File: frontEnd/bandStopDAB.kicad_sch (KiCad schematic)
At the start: 18 parts, among them U401 BGS12P2L6E6327XTSA1, U402 BGS12P2L6E6327XTSA1

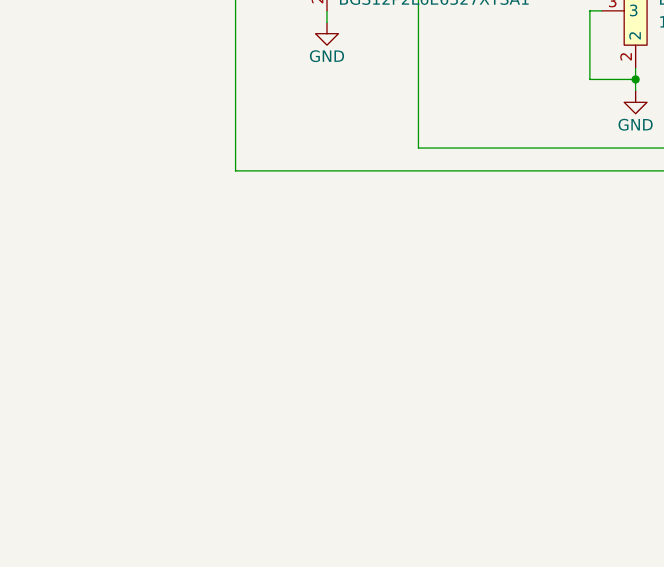
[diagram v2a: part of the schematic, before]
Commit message: add leds for each filter block
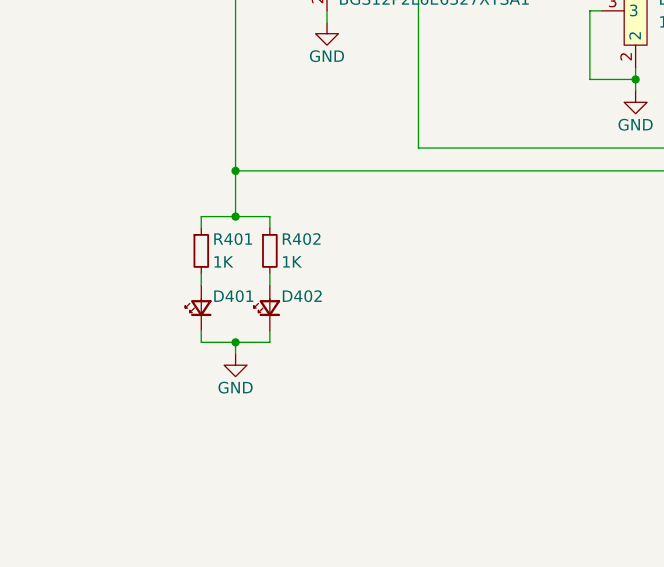
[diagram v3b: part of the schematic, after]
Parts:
- added D401, D402: LED_Small, LED_SMD:LED_0805_2012Metric, symbol Device:LED_Small
- added R401, R402: 1K, Resistor_SMD:R_0805_2012Metric, symbol Device:R_Small
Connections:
- net FILTER_ENABLE: now also R401.1, R402.1
- net GND: now also D401.1 (K), D402.1 (K)
- new net: D401.2 (A), R401.2
- new net: D402.2 (A), R402.2
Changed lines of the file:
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@@
 (kicad_sch (version 20211123) (generator eeschema)
   (paper "A4")
+  (junction (at 60.96 125.73) (diameter 0) (color 0 0 0 0)
+  )
   (junction (at 114.3 74.93) (diameter 0) (color 0 0 0 0)
   )
@@
   (junction (at 180.34 74.93) (diameter 0) (color 0 0 0 0)
   )
+  (junction (at 60.96 106.68) (diameter 0) (color 0 0 0 0)
+  )
   (junction (at 44.45 180.34) (diameter 0) (color 0 0 0 0)
   )
@@
   (junction (at 44.45 172.72) (diameter 0) (color 0 0 0 0)
   )
+  (junction (at 60.96 111.76) (diameter 0) (color 0 0 0 0)
+  )
   (junction (at 204.47 96.52) (diameter 0) (color 0 0 0 0)
   )
@@
     (stroke (width 0) (type default) (color 0 0 0 0))
   )
+  (wire (pts (xy 60.96 106.68) (xy 60.96 111.76))
+    (stroke (width 0) (type default) (color 0 0 0 0))
+  )
   (wire (pts (xy 129.54 81.28) (xy 129.54 74.93))
     (stroke (width 0) (type default) (color 0 0 0 0))
@@
     (stroke (width 0) (type default) (color 0 0 0 0))
   )
+  (wire (pts (xy 57.15 113.03) (xy 57.15 111.76))
+    (stroke (width 0) (type default) (color 0 0 0 0))
+  )
+  (wire (pts (xy 57.15 118.11) (xy 57.15 119.38))
+    (stroke (width 0) (type default) (color 0 0 0 0))
+  )
   (wire (pts (xy 129.54 74.93) (xy 138.43 74.93))
     (stroke (width 0) (type default) (color 0 0 0 0))
@@
     (stroke (width 0) (type default) (color 0 0 0 0))
   )
+  (wire (pts (xy 57.15 125.73) (xy 60.96 125.73))
+    (stroke (width 0) (type default) (color 0 0 0 0))
+  )
   (wire (pts (xy 162.56 71.12) (xy 162.56 74.93))
     (stroke (width 0) (type default) (color 0 0 0 0))
@@
     (stroke (width 0) (type default) (color 0 0 0 0))
   )
+  (wire (pts (xy 60.96 125.73) (xy 60.96 127))
+    (stroke (width 0) (type default) (color 0 0 0 0))
+  )
   (wire (pts (xy 204.47 95.25) (xy 204.47 96.52))
     (stroke (width 0) (type default) (color 0 0 0 0))
@@
     (stroke (width 0) (type default) (color 0 0 0 0))
   )
+  (wire (pts (xy 64.77 111.76) (xy 64.77 113.03))
+    (stroke (width 0) (type default) (color 0 0 0 0))
+  )
+  (wire (pts (xy 60.96 111.76) (xy 64.77 111.76))
+    (stroke (width 0) (type default) (color 0 0 0 0))
+  )
   (wire (pts (xy 134.62 88.9) (xy 133.35 88.9))
     (stroke (width 0) (type default) (color 0 0 0 0))
@@
     (stroke (width 0) (type default) (color 0 0 0 0))
   )
+  (wire (pts (xy 64.77 124.46) (xy 64.77 125.73))
+    (stroke (width 0) (type default) (color 0 0 0 0))
+  )
   (wire (pts (xy 44.45 180.34) (xy 44.45 181.61))
     (stroke (width 0) (type default) (color 0 0 0 0))
@@
     (stroke (width 0) (type default) (color 0 0 0 0))
   )
+  (wire (pts (xy 60.96 125.73) (xy 64.77 125.73))
+    (stroke (width 0) (type default) (color 0 0 0 0))
+  )
   (wire (pts (xy 229.87 88.9) (xy 229.87 90.17))
     (stroke (width 0) (type default) (color 0 0 0 0))
@@
     (stroke (width 0) (type default) (color 0 0 0 0))
   )
+  (wire (pts (xy 64.77 118.11) (xy 64.77 119.38))
+    (stroke (width 0) (type default) (color 0 0 0 0))
+  )
   (wire (pts (xy 195.58 71.12) (xy 195.58 74.93))
     (stroke (width 0) (type default) (color 0 0 0 0))
@@
     (stroke (width 0) (type default) (color 0 0 0 0))
   )
+  (wire (pts (xy 57.15 111.76) (xy 60.96 111.76))
+    (stroke (width 0) (type default) (color 0 0 0 0))
+  )
   (wire (pts (xy 194.31 81.28) (xy 195.58 81.28))
     (stroke (width 0) (type default) (color 0 0 0 0))
@@
   )
   (wire (pts (xy 171.45 96.52) (xy 171.45 97.79))
+    (stroke (width 0) (type default) (color 0 0 0 0))
+  )
+  (wire (pts (xy 57.15 124.46) (xy 57.15 125.73))
     (stroke (width 0) (type default) (color 0 0 0 0))
   )
@@
     (pin "2")
   )
+  (symbol (lib_id "power:GND") (at 60.96 127 0) (unit 1)
+    (in_bom yes) (on_board yes)
+    (property "Reference" "#PWR?" (id 0) (at 60.96 133.35 0)
+      (effects (font (size 1.27 1.27)) hide)
+    )
+    (property "Value" "GND" (id 1) (at 60.96 130.81 0))
+    (property "Footprint" "" (id 2) (at 60.96 127 0)
+      (effects (font (size 1.27 1.27)) hide)
+    )
+    (property "Datasheet" "" (id 3) (at 60.96 127 0)
+      (effects (font (size 1.27 1.27)) hide)
+    )
+    (pin "1")
+  )
   (symbol (lib_id "frontEnd:DIY_COIL") (at 154.94 81.28 0) (unit 1)
     (in_bom yes) (on_board yes)
@@
     (pin "1")
   )
+  (symbol (lib_id "Device:R_Small") (at 57.15 115.57 0) (unit 1)
+    (in_bom yes) (on_board yes)
+    (property "Reference" "R401" (id 0) (at 58.42 114.3 0)
+      (effects (font (size 1.27 1.27)) (justify left))
+    )
+    (property "Value" "1K" (id 1) (at 58.42 116.84 0)
+      (effects (font (size 1.27 1.27)) (justify left))
+    )
+    (property "Footprint" "Resistor_SMD:R_0805_2012Metric" (id 2) (at 57.15 115.57 0)
+      (effects (font (size 1.27 1.27)) hide)
+    )
+    (property "Datasheet" "~" (id 3) (at 57.15 115.57 0)
+      (effects (font (size 1.27 1.27)) hide)
+    )
+    (pin "1")
+    (pin "2")
+  )
   (symbol (lib_id "frontEnd:DIY_COIL") (at 121.92 81.28 0) (unit 1)
     (in_bom yes) (on_board yes)
@@
     (pin "2")
     (pin "3")
+  )
+  (symbol (lib_id "Device:LED_Small") (at 57.15 121.92 90) (unit 1)
+    (in_bom yes) (on_board yes)
+    (property "Reference" "D401" (id 0) (at 58.42 120.65 90)
+      (effects (font (size 1.27 1.27)) (justify right))
+    )
+    (property "Value" "LED_Small" (id 1) (at 59.69 123.1264 90)
+      (effects (font (size 1.27 1.27)) (justify right) hide)
+    )
+    (property "Footprint" "LED_SMD:LED_0805_2012Metric" (id 2) (at 57.15 121.92 90)
+      (effects (font (size 1.27 1.27)) hide)
+    )
+    (property "Datasheet" "~" (id 3) (at 57.15 121.92 90)
+      (effects (font (size 1.27 1.27)) hide)
+    )
+    (pin "1")
+    (pin "2")
   )
   (symbol (lib_id "Device:C_Small") (at 171.45 78.74 0) (unit 1)
@@
     (pin "2")
   )
+  (symbol (lib_id "Device:LED_Small") (at 64.77 121.92 90) (unit 1)
+    (in_bom yes) (on_board yes)
+    (property "Reference" "D402" (id 0) (at 66.04 120.65 90)
+      (effects (font (size 1.27 1.27)) (justify right))
+    )
+    (property "Value" "LED_Small" (id 1) (at 67.31 123.1264 90)
+      (effects (font (size 1.27 1.27)) (justify right) hide)
+    )
+    (property "Footprint" "LED_SMD:LED_0805_2012Metric" (id 2) (at 64.77 121.92 90)
+      (effects (font (size 1.27 1.27)) hide)
+    )
+    (property "Datasheet" "~" (id 3) (at 64.77 121.92 90)
+      (effects (font (size 1.27 1.27)) hide)
+    )
+    (pin "1")
+    (pin "2")
+  )
   (symbol (lib_id "frontEnd:BGS12P2L6E6327XTSA1") (at 236.22 77.47 0) (mirror y) (unit 1)
     (in_bom yes) (on_board yes)
@@
       (effects (font (size 1.27 1.27)) hide)
     )
+    (pin "1")
+    (pin "2")
+  )
+  (symbol (lib_id "Device:R_Small") (at 64.77 115.57 0) (unit 1)
+    (in_bom yes) (on_board yes)
+    (property "Reference" "R402" (id 0) (at 66.04 114.3 0)
+      (effects (font (size 1.27 1.27)) (justify left))
+    )
+    (property "Value" "1K" (id 1) (at 66.04 116.84 0)
+      (effects (font (size 1.27 1.27)) (justify left))
+    )
+    (property "Footprint" "Resistor_SMD:R_0805_2012Metric" (id 2) (at 64.77 115.57 0)
+      (effects (font (size 1.27 1.27)) hide)
+    )
+    (property "Datasheet" "~" (id 3) (at 64.77 115.57 0)
+      (effects (font (size 1.27 1.27)) hide)
+    )

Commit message: assign footprints, part designators
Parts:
- U401, U402: footprint (none) -> frontEnd:BGS12P2L6E6327XTSA1
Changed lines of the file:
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@@
   (symbol (lib_id "power:GND") (at 60.96 127 0) (unit 1)
     (in_bom yes) (on_board yes)
-    (property "Reference" "#PWR?" (id 0) (at 60.96 133.35 0)
+    (property "Reference" "#PWR0175" (id 0) (at 60.96 133.35 0)
       (effects (font (size 1.27 1.27)) hide)
     )
@@
   (symbol (lib_id "power:GND") (at 187.96 86.36 0) (unit 1)
     (in_bom yes) (on_board yes)
-    (property "Reference" "#PWR?" (id 0) (at 187.96 92.71 0)
+    (property "Reference" "#PWR0164" (id 0) (at 187.96 92.71 0)
       (effects (font (size 1.27 1.27)) hide)
     )
@@
   (symbol (lib_id "power:+3V3") (at 44.45 171.45 0) (unit 1)
     (in_bom yes) (on_board yes)
-    (property "Reference" "#PWR?" (id 0) (at 44.45 175.26 0)
+    (property "Reference" "#PWR0174" (id 0) (at 44.45 175.26 0)
       (effects (font (size 1.27 1.27)) hide)
     )
@@
   (symbol (lib_id "power:GND") (at 171.45 97.79 0) (unit 1)
     (in_bom yes) (on_board yes)
-    (property "Reference" "#PWR?" (id 0) (at 171.45 104.14 0)
+    (property "Reference" "#PWR0171" (id 0) (at 171.45 104.14 0)
       (effects (font (size 1.27 1.27)) hide)
     )
@@
   (symbol (lib_id "power:GND") (at 44.45 181.61 0) (unit 1)
     (in_bom yes) (on_board yes)
-    (property "Reference" "#PWR?" (id 0) (at 44.45 187.96 0)
+    (property "Reference" "#PWR0173" (id 0) (at 44.45 187.96 0)
       (effects (font (size 1.27 1.27)) hide)
     )
@@
   (symbol (lib_id "power:+3V3") (at 229.87 68.58 0) (unit 1)
     (in_bom yes) (on_board yes)
-    (property "Reference" "#PWR?" (id 0) (at 229.87 72.39 0)
+    (property "Reference" "#PWR0162" (id 0) (at 229.87 72.39 0)
       (effects (font (size 1.27 1.27)) hide)
     )
@@
   (symbol (lib_id "power:GND") (at 204.47 97.79 0) (unit 1)
     (in_bom yes) (on_board yes)
-    (property "Reference" "#PWR?" (id 0) (at 204.47 104.14 0)
+    (property "Reference" "#PWR0169" (id 0) (at 204.47 104.14 0)
       (effects (font (size 1.27 1.27)) hide)
     )
@@
       (effects (font (size 1.27 1.27)) (justify left))
     )
-    (property "Footprint" "" (id 2) (at 64.77 77.47 0)
+    (property "Footprint" "frontEnd:BGS12P2L6E6327XTSA1" (id 2) (at 64.77 77.47 0)
       (effects (font (size 1.27 1.27)) hide)
     )
@@
   (symbol (lib_id "power:GND") (at 154.94 86.36 0) (unit 1)
     (in_bom yes) (on_board yes)
-    (property "Reference" "#PWR?" (id 0) (at 154.94 92.71 0)
+    (property "Reference" "#PWR0168" (id 0) (at 154.94 92.71 0)
       (effects (font (size 1.27 1.27)) hide)
     )
@@
   (symbol (lib_id "power:GND") (at 138.43 97.79 0) (unit 1)
     (in_bom yes) (on_board yes)
-    (property "Reference" "#PWR?" (id 0) (at 138.43 104.14 0)
+    (property "Reference" "#PWR0170" (id 0) (at 138.43 104.14 0)
       (effects (font (size 1.27 1.27)) hide)
     )
@@
       (effects (font (size 1.27 1.27)) (justify right))
     )
-    (property "Footprint" "" (id 2) (at 236.22 77.47 0)
+    (property "Footprint" "frontEnd:BGS12P2L6E6327XTSA1" (id 2) (at 236.22 77.47 0)
       (effects (font (size 1.27 1.27)) hide)
     )
@@
   (symbol (lib_id "power:GND") (at 121.92 86.36 0) (unit 1)
     (in_bom yes) (on_board yes)
-    (property "Reference" "#PWR?" (id 0) (at 121.92 92.71 0)
+    (property "Reference" "#PWR0165" (id 0) (at 121.92 92.71 0)
       (effects (font (size 1.27 1.27)) hide)
     )
@@
   (symbol (lib_id "power:+3V3") (at 71.12 68.58 0) (unit 1)
     (in_bom yes) (on_board yes)
-    (property "Reference" "#PWR?" (id 0) (at 71.12 72.39 0)
+    (property "Reference" "#PWR0166" (id 0) (at 71.12 72.39 0)
       (effects (font (size 1.27 1.27)) hide)
     )
@@
   (symbol (lib_id "power:GND") (at 105.41 97.79 0) (unit 1)
     (in_bom yes) (on_board yes)
-    (property "Reference" "#PWR?" (id 0) (at 105.41 104.14 0)
+    (property "Reference" "#PWR0172" (id 0) (at 105.41 104.14 0)
       (effects (font (size 1.27 1.27)) hide)
     )
@@
   (symbol (lib_id "power:GND") (at 229.87 90.17 0) (unit 1)
     (in_bom yes) (on_board yes)
-    (property "Reference" "#PWR?" (id 0) (at 229.87 96.52 0)
+    (property "Reference" "#PWR0163" (id 0) (at 229.87 96.52 0)
       (effects (font (size 1.27 1.27)) hide)
     )
@@
   (symbol (lib_id "power:GND") (at 71.12 90.17 0) (unit 1)
     (in_bom yes) (on_board yes)
-    (property "Reference" "#PWR?" (id 0) (at 71.12 96.52 0)
-      (effects (font (size 1.27 1.27)) hide)
-    )
+    (property "Reference" "#PWR0167" (id 0) (at 71.12 96.52 0)
+      (effects (font (size 1.27 1.27)) hide)
+    )

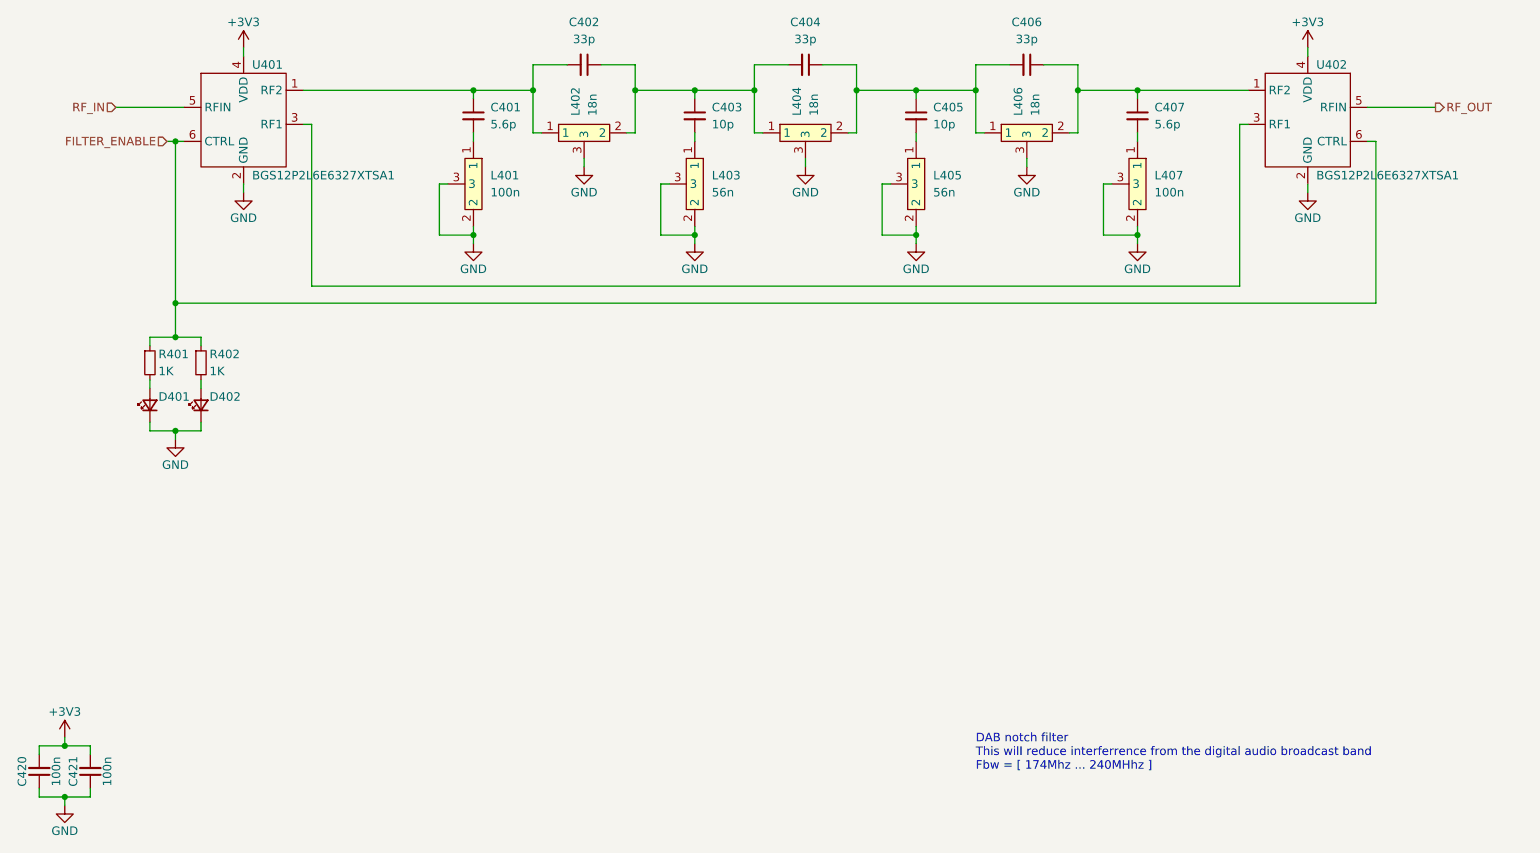
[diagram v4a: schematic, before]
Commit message: convert all embeded filter to plug-in modules, start pcb layout
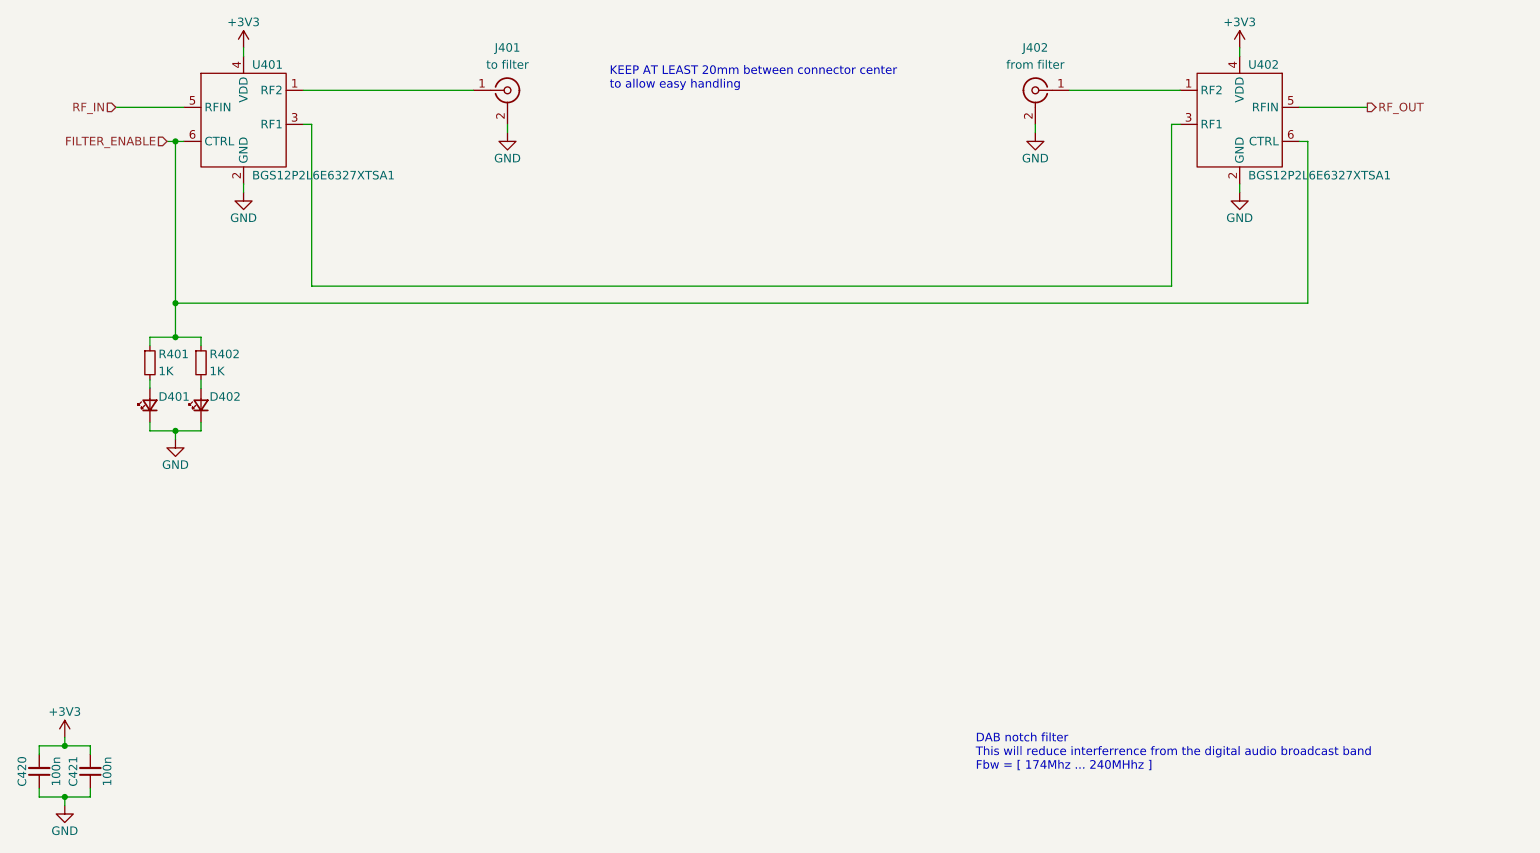
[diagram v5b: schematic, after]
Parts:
- removed C401, C407: 5.6p, Capacitor_SMD:C_0805_2012Metric, symbol Device:C_Small
- removed C402, C404, C406: 33p, Capacitor_SMD:C_0805_2012Metric, symbol Device:C_Small
- removed C403, C405: 10p, Capacitor_SMD:C_0805_2012Metric, symbol Device:C_Small
- removed L401, L407: 100n, frontEnd:COIL, symbol frontEnd:DIY_COIL
- removed L402, L404, L406: 18n, frontEnd:COIL, symbol frontEnd:DIY_COIL
- removed L403, L405: 56n, frontEnd:COIL, symbol frontEnd:DIY_COIL
- added J401: to filter, frontEnd:SMA_FEM_TH_VERTICAL, symbol Connector:Conn_Coaxial
- added J402: from filter, frontEnd:SMA_FEM_TH_VERTICAL, symbol Connector:Conn_Coaxial
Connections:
- net GND: now also J401.2 (Ext), J402.2 (Ext)
- net at U401.1 (RF2): now also J401.1 (In)
- net at U402.1 (RF2): now also J402.1 (In)
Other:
- note added: "KEEP AT LEAST 20mm between connector center to allow easy handling"
- moved on the sheet: U402
